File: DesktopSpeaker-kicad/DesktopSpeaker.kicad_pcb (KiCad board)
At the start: 4 copper layers, 116 x 138 mm, 315 parts, among them J1 USB_C_Receptacle_USB2.0_16P, J10 B2P-VH, J11 B2P-VH, J2 HEAD_OUT, J3 AUX_IN, J4 I2C service, J5 1S_PACK_3PIN, J6 SWD, J7 SWD_TC2030, J8 BM83_PROG, J9 B2P-VH, Q100 2N7002, Q101 2N7002, Q102 2N7002, Q103 CSD17579Q3A, Q104 2N7002, SW100 WAKE_QON, SW101 BAT_DISCONNECT, U1 BM83SM1-00TA, U10 TPA6132A2RTER, U11 TPS25730DREFR, U12 TPS7A0230PDBVR, U13 TS5A3167DBVR, U14 TPS63802DLAR, U15 TPS63802DLAR, U16 TS5A3167DBVR, U17 TS5A3167DBVR, U19 TPS7B8450QWDRBRQ1, U2 PCM2902CDBR, U20 TPS2116DRLR, U21 TPS3839G33DBZR, U22 TPS7A2033PDBVR, U23 TPS22917DBVR, U24 PCM1862DBTR, U25 TPS61088RHLR, U3 STM32G071RBT6, U4 BQ25792RQMR, U5 MAX17048G+T10, U6 TAS5825MRHBR, U7 TAS5825MRHBR, U8 TS5A23157DGSR, U9 TS5A23157DGSR, Y170 12MHz, Y200 24.576MHz

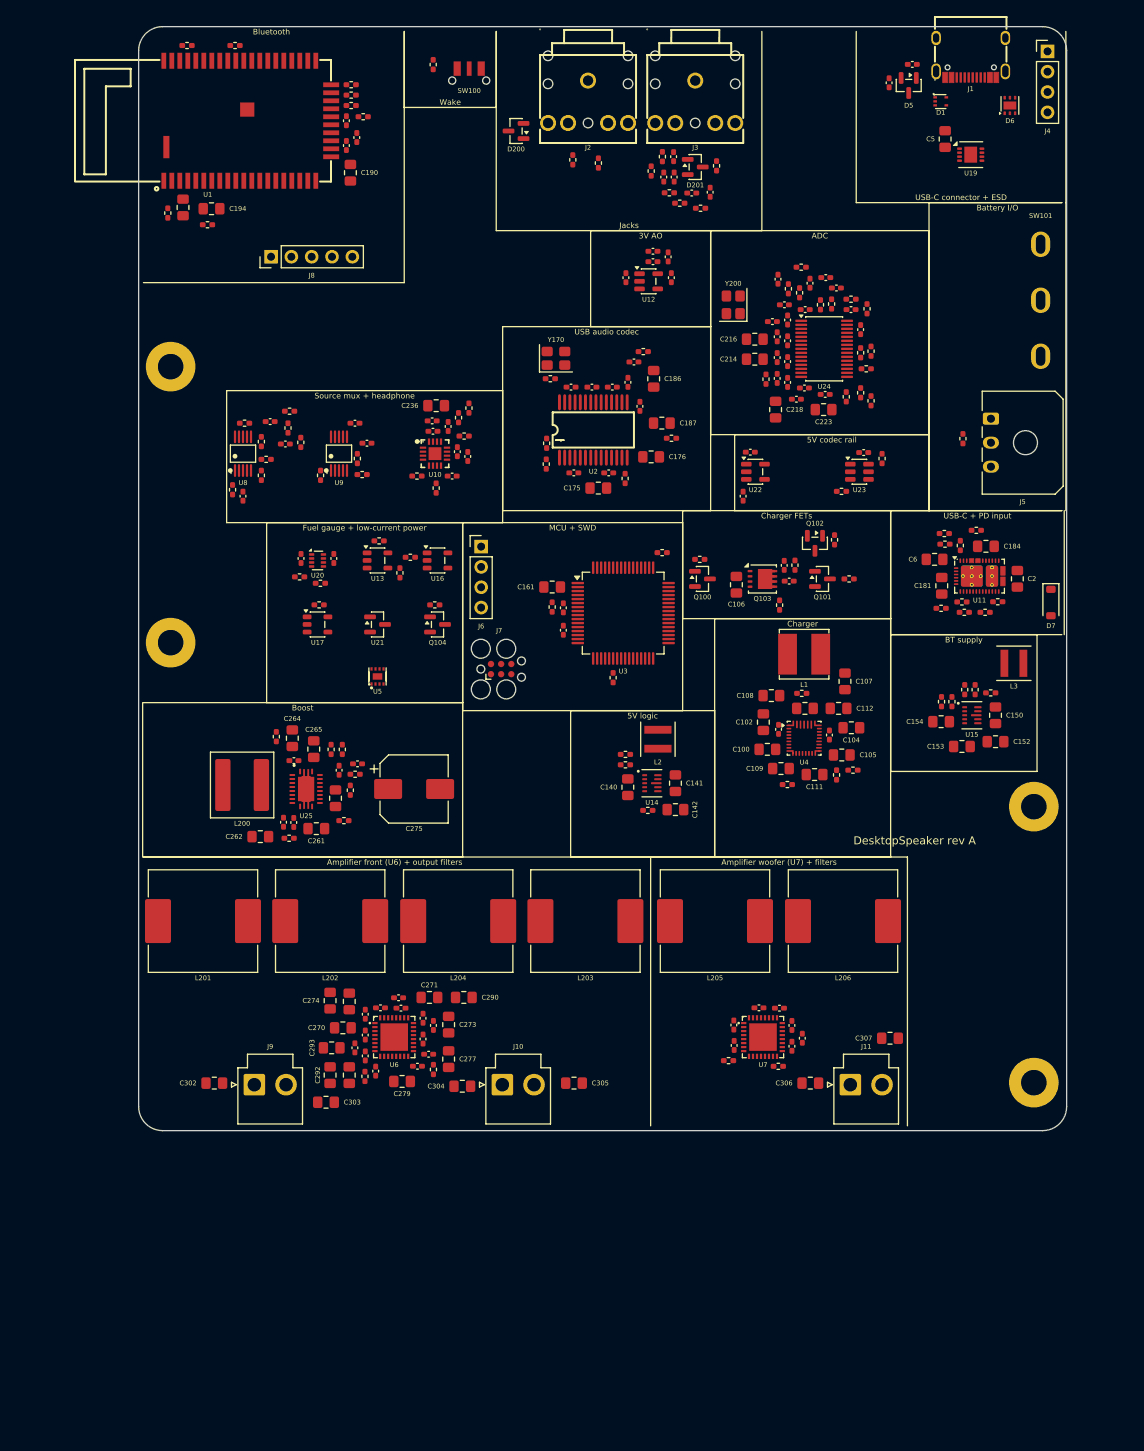
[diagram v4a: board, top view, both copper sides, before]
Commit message: Placement v8: sequence-pair compaction, 121x127 mm, 10 PTH GND mounting holes, larger section titles; CAD refit (0 overlaps)
Co-Authored-By: Claude Sonnet 5.5 <noreply@anthropic.com>
Claude-Session: https://claude.ai/code/session_01N5RHheWSjDFDPbKVD5YVeJ
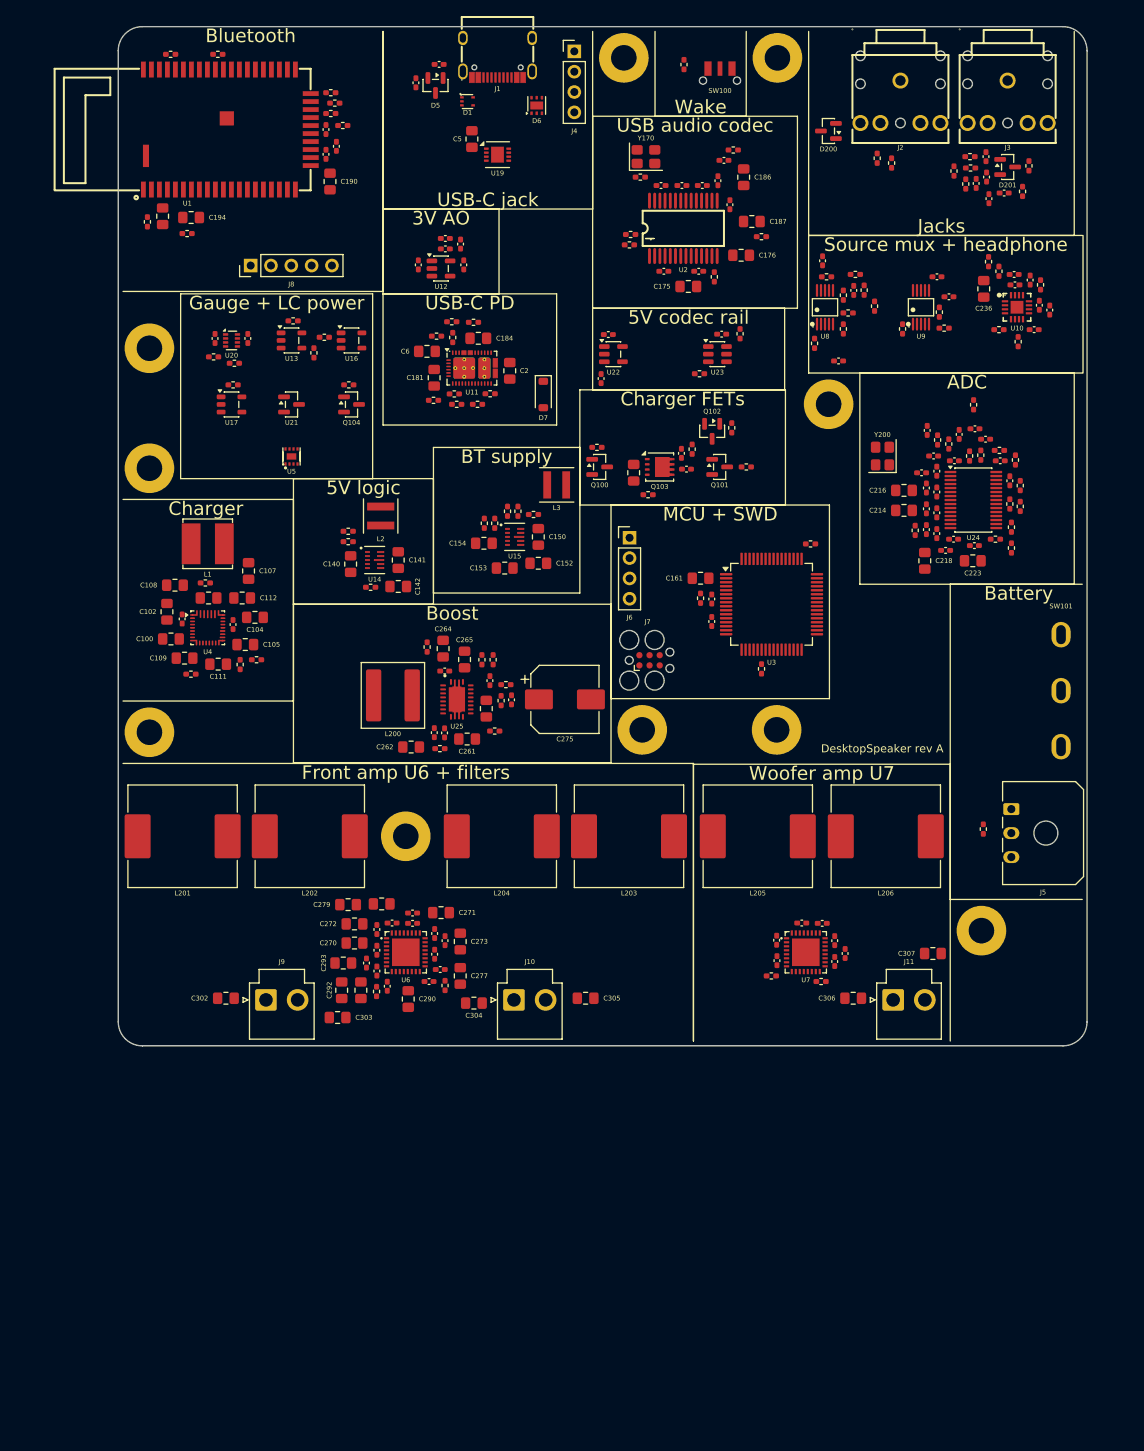
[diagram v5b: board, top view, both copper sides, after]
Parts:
- added H5: M3 PTH GND, DesktopSpeaker:MountingHole_3.2mm_M3_PTH_GND, F.Cu at (171.8, 107.9)
- added H6: M3 PTH GND, DesktopSpeaker:MountingHole_3.2mm_M3_PTH_GND, F.Cu at (154.9, 107.9)
- added H7: M3 PTH GND, DesktopSpeaker:MountingHole_3.2mm_M3_PTH_GND, F.Cu at (93.3, 108.2)
- added H8: M3 PTH GND, DesktopSpeaker:MountingHole_3.2mm_M3_PTH_GND, F.Cu at (93.3, 75.2)
- added H9: M3 PTH GND, DesktopSpeaker:MountingHole_3.2mm_M3_PTH_GND, F.Cu at (93.3, 60.2)
- added HA1: M3 PTH GND, DesktopSpeaker:MountingHole_3.2mm_M3_PTH_GND, F.Cu at (125.4, 121.2)
- moved H4 138.0 mm to (152.7, 23.9)
- moved H2 107.6 mm to (197.3, 133.0)
- moved H3 98.9 mm to (171.8, 23.9)
- moved H1 82.4 mm to (178.2, 67.2)
- moved C232 76.3 mm to (179.5, 61.8), turned to 180 degrees
- moved C105 75.8 mm to (105.3, 97.2)
- moved C110 75.8 mm to (103.8, 94.7)
- moved R100 75.8 mm to (104.7, 99.7)
- moved C103 75.8 mm to (97.4, 94.0)
- moved C108 75.8 mm to (96.5, 89.8)
- moved C111 75.8 mm to (101.9, 99.7)
- moved C112 75.8 mm to (104.9, 91.4)
- moved C100 75.8 mm to (96.0, 96.5)
- moved C101 75.8 mm to (100.7, 91.4)
- moved C102 75.8 mm to (95.5, 93.1)
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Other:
- board size 116 x 138 mm -> 121.1 x 127.4 mm
- board text added: "Battery"
- board text added: "Front amp U6 + filters"
- board text added: "Gauge + LC power"
- board text added: "USB-C PD"
- board text added: "USB-C jack"
- board text added: "Woofer amp U7"
- board text removed: "Amplifier front (U6) + output filters"
- board text removed: "Amplifier woofer (U7) + filters"
- board text removed: "Battery I/O"
- board text removed: "Fuel gauge + low-current power"
- board text removed: "USB-C + PD input"
- board text removed: "USB-C connector + ESD"

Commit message: Placement v9: EC11E volume encoder, 25 test points, silkscreen pass (closed sections, border, hole squares, labels), Orwellian logo on back, CAD refit
Co-Authored-By: Claude Sonnet 5.5 <noreply@anthropic.com>
Claude-Session: https://claude.ai/code/session_016fe4xPJbEE2SjGafuyNLjb
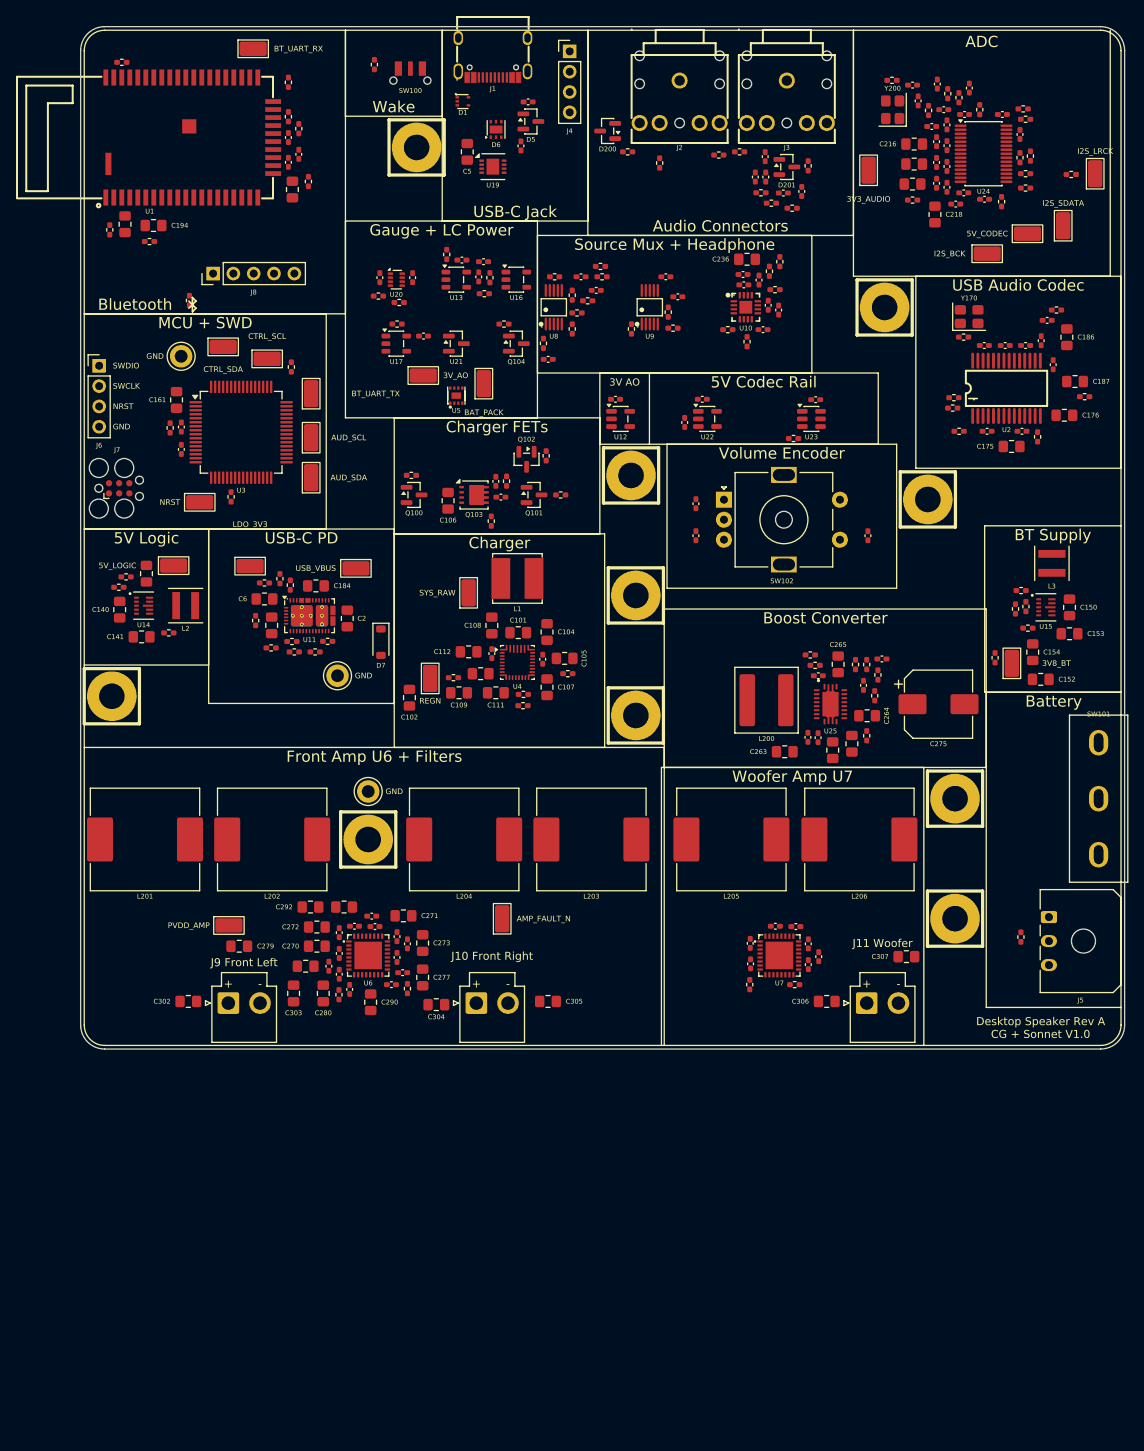
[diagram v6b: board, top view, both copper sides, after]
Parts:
- added C308: 10nF, DesktopSpeaker:C_0402_1005Metric_Pad0.74x0.62mm_HandSolder, F.Cu at (161.7, 79.6)
- added C309: 10nF, DesktopSpeaker:C_0402_1005Metric_Pad0.74x0.62mm_HandSolder, F.Cu at (161.7, 83.6)
- added C310: 10nF, DesktopSpeaker:C_0402_1005Metric_Pad0.74x0.62mm_HandSolder, F.Cu at (183.2, 83.6)
- added LOGO1: Orwellian Industries, DesktopSpeaker:Logo_Orwellian, B.Cu at (117.5, 104.2)
- added SW102: EC11E, DesktopSpeaker:RotaryEncoder_Alps_EC11E-Switch_Vertical_H20mm_MountingHoles, F.Cu at (165.2, 79.1)
- added TP1: USB_VBUS, DesktopSpeaker:TestPoint_Keystone_5015_Micro_Mini, F.Cu at (119.2, 87.7)
- added TP10: PVDD_AMP, DesktopSpeaker:TestPoint_Keystone_5015_Micro_Mini, F.Cu at (103.3, 132.4)
- added TP11: REGN, DesktopSpeaker:TestPoint_Keystone_5015_Micro_Mini, F.Cu at (128.4, 101.5)
- added TP12: I2S_BCK, DesktopSpeaker:TestPoint_Keystone_5015_Micro_Mini, F.Cu at (198.1, 48.4)
- added TP13: I2S_LRCK, DesktopSpeaker:TestPoint_Keystone_5015_Micro_Mini, F.Cu at (211.6, 38.4)
- added TP14: I2S_SDATA, DesktopSpeaker:TestPoint_Keystone_5015_Micro_Mini, F.Cu at (207.6, 44.9)
- added TP15: CTRL_SDA, DesktopSpeaker:TestPoint_Keystone_5015_Micro_Mini, F.Cu at (102.6, 60.0)
- added TP16: CTRL_SCL, DesktopSpeaker:TestPoint_Keystone_5015_Micro_Mini, F.Cu at (108.1, 61.5)
- added TP17: AUD_SDA, DesktopSpeaker:TestPoint_Keystone_5015_Micro_Mini, F.Cu at (113.6, 76.4)
- added TP18: AUD_SCL, DesktopSpeaker:TestPoint_Keystone_5015_Micro_Mini, F.Cu at (113.6, 71.4)
- added TP19: NRST, DesktopSpeaker:TestPoint_Keystone_5015_Micro_Mini, F.Cu at (99.6, 79.5)
- added TP2: SYS_RAW, DesktopSpeaker:TestPoint_Keystone_5015_Micro_Mini, F.Cu at (133.2, 90.8)
- added TP20: AMP_FAULT_N, DesktopSpeaker:TestPoint_Keystone_5015_Micro_Mini, F.Cu at (137.4, 131.5)
- added TP21: BT_UART_TX, DesktopSpeaker:TestPoint_Keystone_5015_Micro_Mini, F.Cu at (113.6, 65.9)
- added TP22: BT_UART_RX, DesktopSpeaker:TestPoint_Keystone_5015_Micro_Mini, F.Cu at (106.3, 22.8)
- added TP23: GND, DesktopSpeaker:TestPoint_Keystone_5010-5014_Multipurpose, F.Cu at (116.9, 101.1)
- added TP24: GND, DesktopSpeaker:TestPoint_Keystone_5010-5014_Multipurpose, F.Cu at (120.7, 115.6)
- added TP25: GND, DesktopSpeaker:TestPoint_Keystone_5010-5014_Multipurpose, F.Cu at (97.3, 61.2)
- added TP3: BAT_PACK, DesktopSpeaker:TestPoint_Keystone_5015_Micro_Mini, F.Cu at (135.1, 64.6)
- added TP4: 3V_AO, DesktopSpeaker:TestPoint_Keystone_5015_Micro_Mini, F.Cu at (127.6, 63.6)
- added TP5: LDO_3V3, DesktopSpeaker:TestPoint_Keystone_5015_Micro_Mini, F.Cu at (105.9, 87.4)
- added TP6: 3V3_AUDIO, DesktopSpeaker:TestPoint_Keystone_5015_Micro_Mini, F.Cu at (183.2, 38.0)
- added TP7: 5V_LOGIC, DesktopSpeaker:TestPoint_Keystone_5015_Micro_Mini, F.Cu at (96.4, 87.4)
- added TP8: 5V_CODEC, DesktopSpeaker:TestPoint_Keystone_5015_Micro_Mini, F.Cu at (203.1, 45.9)
- added TP9: 3V8_BT, DesktopSpeaker:TestPoint_Keystone_5015_Micro_Mini, F.Cu at (201.2, 99.6)
- moved H8 115.4 mm to (194.1, 131.5)
- moved H7 101.0 mm to (194.1, 116.5)
- moved H1 96.7 mm to (88.7, 103.7)
- moved H9 92.0 mm to (185.2, 55.1)
- moved C153 71.1 mm to (208.4, 95.9), turned to 0 degrees
- moved C154 69.9 mm to (203.8, 98.2), turned to 90 degrees
- moved C162 69.7 mm to (97.3, 72.8)
- moved J6 69.7 mm to (87.1, 62.4)
- moved J7 69.7 mm to (89.6, 77.7)
- moved R259 69.7 mm to (103.6, 78.8)
- moved U3 69.7 mm to (104.8, 70.7)
- moved C160 69.7 mm to (97.3, 70.0)
- moved R106 69.6 mm to (95.9, 70.2)
- moved C161 69.2 mm to (96.7, 66.7), turned to 90 degrees
- moved R160 68.6 mm to (111.1, 62.5), turned to 90 degrees
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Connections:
- U3 pad 48: unconnected-(U3-PC8-Pad48) -> /MCU/ENC_A
- U3 pad 49: unconnected-(U3-PC9-Pad49) -> /MCU/ENC_B
- U3 pad 64: unconnected-(U3-PC10-Pad64) -> /MCU/ENC_SW
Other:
- board size 121.1 x 127.4 mm -> 130.5 x 127.8 mm
- board text added: "+"
- board text added: "-"
- board text added: "3V3_AUDIO"
- board text added: "3V8_BT"
- board text added: "3V_AO"
- board text added: "5V Codec Rail"
- board text added: "5V Logic"
- board text added: "5V_CODEC"
- board text added: "5V_LOGIC"
- board text added: "AMP_FAULT_N"
- board text added: "AUD_SCL"
- board text added: "AUD_SDA"
- board text added: "Audio Connectors"
- board text added: "BAT_PACK"
- board text added: "BT Supply"
- board text added: "BT_UART_RX"
- board text added: "BT_UART_TX"
- board text added: "Boost Converter"
- board text added: "CG + Sonnet V1.0"
- board text added: "CTRL_SCL"
- board text added: "CTRL_SDA"
- board text added: "Desktop Speaker Rev A"
- board text added: "Front Amp U6 + Filters"
- board text added: "GND"
- board text added: "Gauge + LC Power"
- board text added: "I2S_BCK"
- board text added: "I2S_LRCK"
- board text added: "I2S_SDATA"
- board text added: "J10 Front Right"
- board text added: "J11 Woofer"
- board text added: "J9 Front Left"
- board text added: "LDO_3V3"
- board text added: "NRST"
- board text added: "PVDD_AMP"
- board text added: "REGN"
- board text added: "SWCLK"
- board text added: "SWDIO"
- board text added: "SYS_RAW"
- board text added: "Source Mux + Headphone"
- board text added: "USB Audio Codec"
- board text added: "USB-C Jack"
- board text added: "USB_VBUS"
- board text added: "Volume Encoder"
- board text added: "Woofer Amp U7"
- board text removed: "5V codec rail"
- board text removed: "5V logic"
- board text removed: "BT supply"
- board text removed: "Boost"
- board text removed: "DesktopSpeaker rev A"
- board text removed: "DesktopSpeaker rev A 2026-10-06 (placement only)"
- board text removed: "Front amp U6 + filters"
- board text removed: "Gauge + LC power"
- board text removed: "Jacks"
- board text removed: "Source mux + headphone"
- board text removed: "USB audio codec"
- board text removed: "USB-C jack"
- board text removed: "Woofer amp U7"
